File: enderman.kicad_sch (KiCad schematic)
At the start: 23 parts, among them U1 4030, U2 LM556

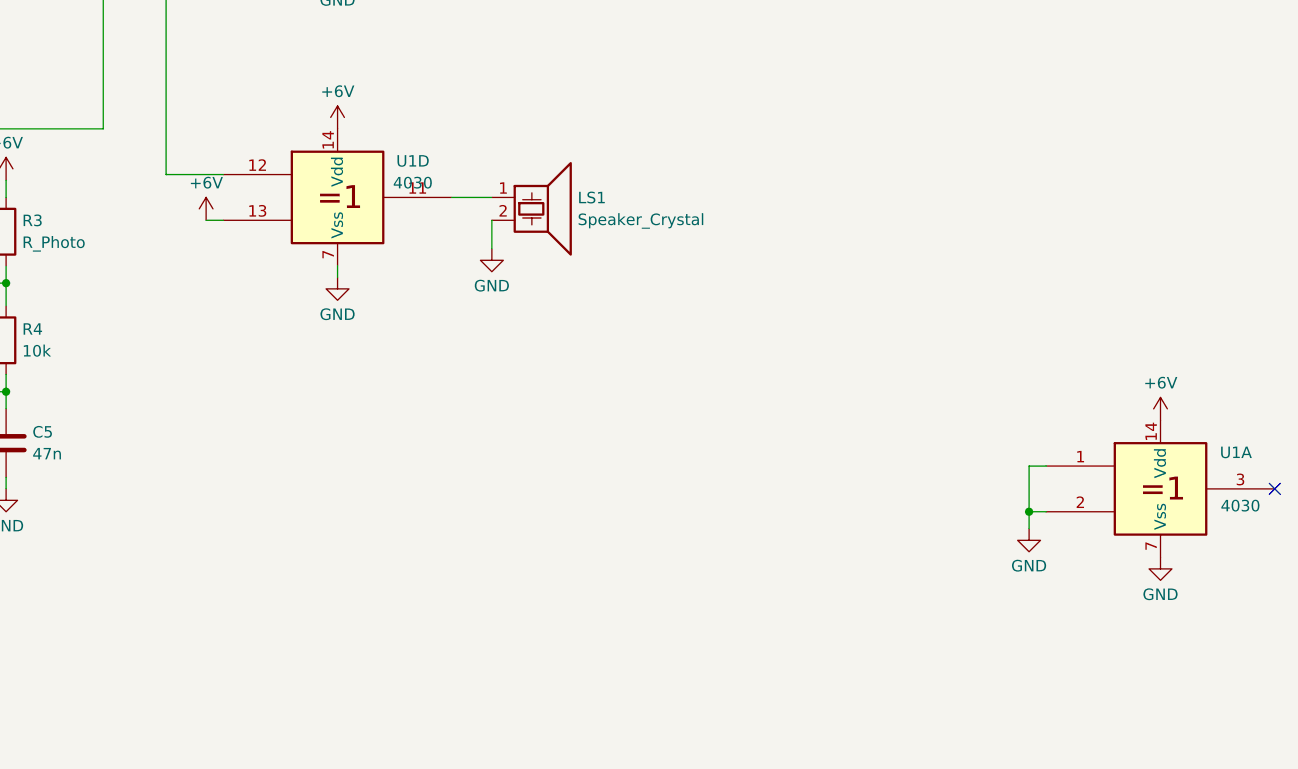
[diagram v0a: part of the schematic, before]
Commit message: add option for 2x drive to buzzer
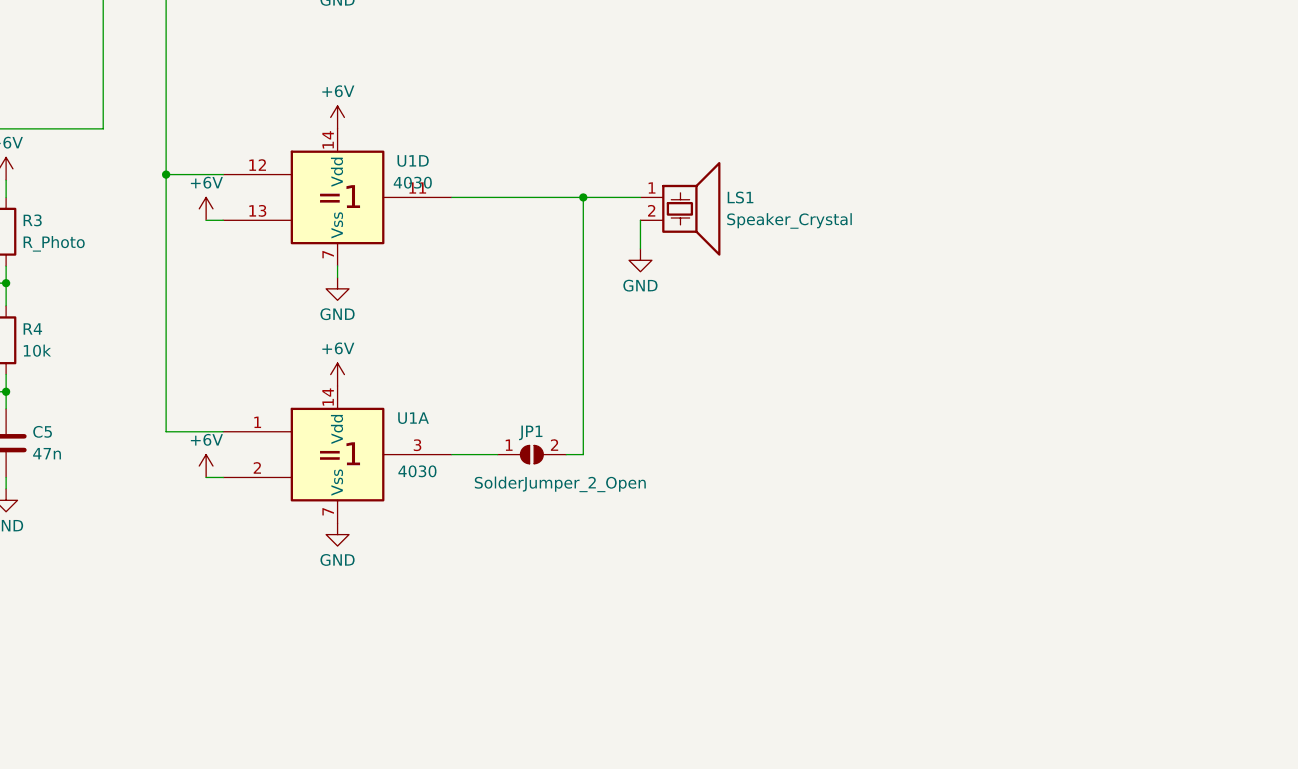
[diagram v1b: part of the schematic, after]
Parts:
- added JP1: SolderJumper_2_Open, symbol Jumper:SolderJumper_2_Open
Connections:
- net +6V: now also U1.2
- net GND: no longer U1.1, U1.2
- net at D1.1 (K), U1.12, U1.4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: now also U1.1
- net at U1.3: now also JP1.1 (A)
- net at LS1.1, U1.11: now also JP1.2 (B)
- no-connect marks 3 -> 2
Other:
- moved on the sheet: LS1, U1A
